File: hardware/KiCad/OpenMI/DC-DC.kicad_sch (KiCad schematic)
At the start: 37 parts, among them Q4 GAN7R0-150LBEZ, Q5 GAN7R0-150LBEZ, U3 1EDN7550B, U4 1EDN7550B

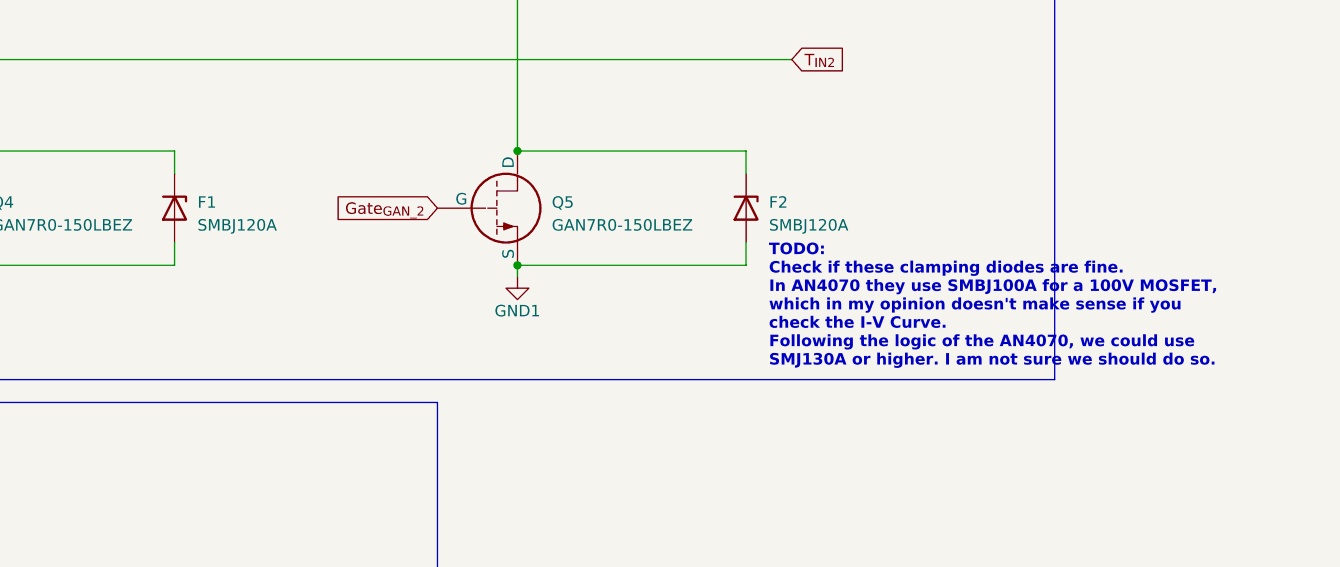
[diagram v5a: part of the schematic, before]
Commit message: fix(hw): change GaN FET protection from `SMBJ120A` to `SMBJ100A`
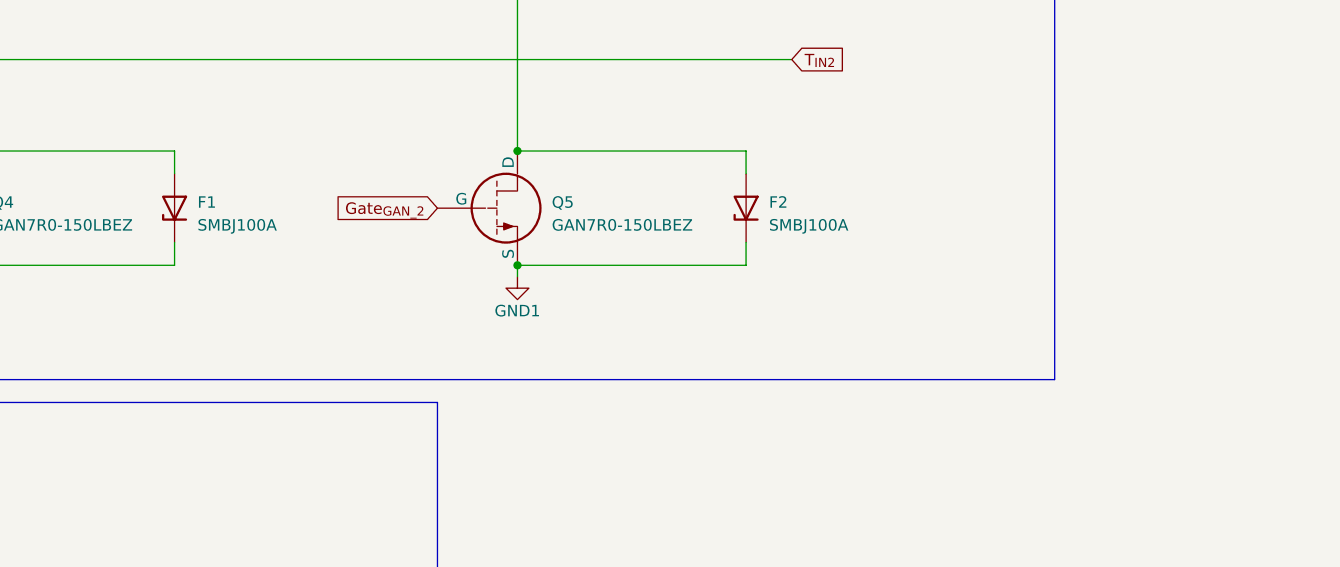
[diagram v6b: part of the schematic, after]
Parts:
- removed F1, F2: SMBJ120A, Diode_SMD:D_SMB, symbol _Diode_TVS:SMBJ120A
- added F1, F2: SMBJ100A, Diode_SMD:D_SMB, symbol _Diode_TVS:SMBJ100A
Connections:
- net GND1: now also F1.1 (K), F2.1 (K)
- net T_{IN1}: now also F2.2 (A)
- net T_{IN2}: now also F1.2 (A)
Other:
- note removed: "TODO: Check if these clamping diodes are fine. In AN4070 they use SMBJ100A for a 100V MOSFET, which in my opinion doesn't make sense if you check the I-V Curve. Following the logic of the AN4070, we could use SMJ130A or higher. I am not sure we should do so."
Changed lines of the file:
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@@
     (effects (font (size 1.27 1.27)) (justify left bottom))
-  )
-  (text "TODO:\nCheck if these clamping diodes are fine.\nIn AN4070 they use SMBJ100A for a 100V MOSFET,\nwhich in my opinion doesn't make sense if you \ncheck the I-V Curve.\nFollowing the logic of the AN4070, we could use\nSMJ130A or higher. I am not sure we should do so."
-    (at 336.55 160.02 0)
-    (effects (font (size 1.27 1.27) bold (color 255 0 0 1)) (justify left bottom))
   )
   (text "The GAN7R0-150LBEZ has a input capacitance of \n C_{iss} = 865 pF\nThe gate driver 1EDN7550B has rise times of\n t_{rise_1.8nF} = 6.5 ns\n t_{rise_200pF} = 1 ns\nSo using the GAN7R0-150LBEZ with the 1EDN7550B we can roughly asume:\n t_{rise_865pf} = (6.5 ns - 1 ns) / (1800 pF - 200 pF) * 865 pF  \n            = 2.97 ns\nThis results in\n  t_{charge_QGS} = 2.97 ns + 1.7 nC / 4 A  = 3.395 ns,\nwhich is\n  t_{charge_QGS} / T_{on_minimal} = 3.395 ns / 2000 ns ≈ 0.0017,\nso the rise time is at maximum 0.17% of the period time.\nThe results for the fall time should be roughly similar.\n\nSimulating this in LTSpice with\n  R_{Gate_SNK} = 2.2 Ω\n  R_{Gate_SRC} = 0.5 Ω\nresults in the following times (measuring V_{GS} from 10% to 90%)\n  t_{charge_QGS} = 8.44 ns     → 0.42% of period time\n  t_{discharge_QGS} = 2.59 ns   → 0.13% of period time"
@@
     )
   )
+  (symbol (lib_id "_Diode_TVS:SMBJ100A") (at 334.01 142.24 90) (unit 1)
+    (in_bom yes) (on_board yes) (dnp no) (fields_autoplaced)
+    (property "Reference" "F2" (at 336.55 141.605 90)
+      (effects (font (size 1.27 1.27)) (justify right))
+    )
+    (property "Value" "SMBJ100A" (at 336.55 144.145 90)
+      (effects (font (size 1.27 1.27)) (justify right))
+    )
+    (property "Footprint" "Diode_SMD:D_SMB" (at 334.01 142.24 0)
+      (effects (font (size 1.27 1.27)) hide)
+    )
+    (property "Datasheet" "https://www.mouser.de/datasheet/2/240/Littelfuse_TVS_Diode_SMBJ_Datasheet_pdf-1108540.pdf" (at 334.01 142.24 0)
+      (effects (font (size 1.27 1.27)) hide)
+    )
+    (property "MF" "Littelfuse" (at 334.01 142.24 0)
+      (effects (font (size 1.27 1.27)) hide)
+    )
+    (property "MPN" "SMBJ100A" (at 334.01 142.24 0)
+      (effects (font (size 1.27 1.27)) hide)
+    )
+    (property "OC_CONRAD" "" (at 334.01 142.24 0)
+      (effects (font (size 1.27 1.27)) hide)
+    )
+    (property "OC_FARNELL" "" (at 334.01 142.24 0)
+      (effects (font (size 1.27 1.27)) hide)
+    )
+    (property "OC_LCSC" "C151249" (at 334.01 142.24 0)
+      (effects (font (size 1.27 1.27)) hide)
+    )
+    (property "OC_MOUSER" "576-SMBJ100A" (at 334.01 142.24 0)
+      (effects (font (size 1.27 1.27)) hide)
+    )
+    (property "OC_REICHELT" "" (at 334.01 142.24 0)
+      (effects (font (size 1.27 1.27)) hide)
+    )
+    (pin "1")
+    (pin "2")
+    (instances
+      (project "OpenMI"
+        (path "/2d959e19-1572-42a0-a8fd-da8463ad4e66/efbfb180-c2bb-45aa-ab04-e5a4cb37fddc"
+          (reference "F2") (unit 1)
+        )
+      )
+    )
+  )
   (symbol (lib_id "power:+5V") (at 270.51 72.39 0) (unit 1)
     (in_bom yes) (on_board yes) (dnp no) (fields_autoplaced)
@@
         (path "/2d959e19-1572-42a0-a8fd-da8463ad4e66/efbfb180-c2bb-45aa-ab04-e5a4cb37fddc"
           (reference "R25") (unit 1)
+        )
+      )
+    )
+  )
+  (symbol (lib_id "_Diode_TVS:SMBJ100A") (at 270.51 142.24 90) (unit 1)
+    (in_bom yes) (on_board yes) (dnp no) (fields_autoplaced)
+    (property "Reference" "F1" (at 273.05 141.605 90)
+      (effects (font (size 1.27 1.27)) (justify right))
+    )
+    (property "Value" "SMBJ100A" (at 273.05 144.145 90)
+      (effects (font (size 1.27 1.27)) (justify right))
+    )
+    (property "Footprint" "Diode_SMD:D_SMB" (at 270.51 142.24 0)
+      (effects (font (size 1.27 1.27)) hide)
+    )
+    (property "Datasheet" "https://www.mouser.de/datasheet/2/240/Littelfuse_TVS_Diode_SMBJ_Datasheet_pdf-1108540.pdf" (at 270.51 142.24 0)
+      (effects (font (size 1.27 1.27)) hide)
+    )
+    (property "MF" "Littelfuse" (at 270.51 142.24 0)
+      (effects (font (size 1.27 1.27)) hide)
+    )
+    (property "MPN" "SMBJ100A" (at 270.51 142.24 0)
+      (effects (font (size 1.27 1.27)) hide)
+    )
+    (property "OC_CONRAD" "" (at 270.51 142.24 0)
+      (effects (font (size 1.27 1.27)) hide)
+    )
+    (property "OC_FARNELL" "" (at 270.51 142.24 0)
+      (effects (font (size 1.27 1.27)) hide)
+    )
+    (property "OC_LCSC" "C151249" (at 270.51 142.24 0)
+      (effects (font (size 1.27 1.27)) hide)
+    )
+    (property "OC_MOUSER" "576-SMBJ100A" (at 270.51 142.24 0)
+      (effects (font (size 1.27 1.27)) hide)
+    )
+    (property "OC_REICHELT" "" (at 270.51 142.24 0)
+      (effects (font (size 1.27 1.27)) hide)
+    )
+    (pin "1")
+    (pin "2")
+    (instances
+      (project "OpenMI"
+        (path "/2d959e19-1572-42a0-a8fd-da8463ad4e66/efbfb180-c2bb-45aa-ab04-e5a4cb37fddc"
+          (reference "F1") (unit 1)
         )
       )
@@
         )
       )
-    )
-  )
-  (symbol (lib_id "_Diode_TVS:SMBJ120A") (at 334.01 142.24 270) (unit 1)
-    (in_bom yes) (on_board yes) (dnp no) (fields_autoplaced)
-    (property "Reference" "F2" (at 336.55 141.605 90)
-      (effects (font (size 1.27 1.27)) (justify left))
-    )
-    (property "Value" "SMBJ120A" (at 336.55 144.145 90)
-      (effects (font (size 1.27 1.27)) (justify left))
-    )
-    (property "Footprint" "Diode_SMD:D_SMB" (at 334.01 142.24 0)
-      (effects (font (size 1.27 1.27)) hide)
-    )
-    (property "Datasheet" "https://www.mouser.de/datasheet/2/240/Littelfuse_TVS_Diode_SMBJ_Datasheet_pdf-1108540.pdf" (at 334.01 142.24 0)
-      (effects (font (size 1.27 1.27)) hide)
-    )
-    (property "MF" "Littelfuse" (at 334.01 142.24 0)
-      (effects (font (size 1.27 1.27)) hide)
-    )
-    (property "MPN" "SMBJ120A" (at 334.01 142.24 0)
-      (effects (font (size 1.27 1.27)) hide)
-    )
-    (property "OC_CONRAD" "" (at 334.01 142.24 0)
-      (effects (font (size 1.27 1.27)) hide)
-    )
-    (property "OC_FARNELL" "" (at 334.01 142.24 0)
-      (effects (font (size 1.27 1.27)) hide)
-    )
-    (property "OC_LCSC" "C224005" (at 334.01 142.24 0)
-      (effects (font (size 1.27 1.27)) hide)
-    )
-    (property "OC_MOUSER" "576-SMBJ120A" (at 334.01 142.24 0)
-      (effects (font (size 1.27 1.27)) hide)
-    )
-    (property "OC_REICHELT" "" (at 334.01 142.24 0)
-      (effects (font (size 1.27 1.27)) hide)
-    )
-    (pin "1")
-    (pin "2")
-    (instances
-      (project "OpenMI"
-        (path "/2d959e19-1572-42a0-a8fd-da8463ad4e66/efbfb180-c2bb-45aa-ab04-e5a4cb37fddc"
-          (reference "F2") (unit 1)
-        )
-      )
-    )
-  )
-  (symbol (lib_id "_Diode_TVS:SMBJ120A") (at 270.51 142.24 270) (unit 1)
-    (in_bom yes) (on_board yes) (dnp no) (fields_autoplaced)
-    (property "Reference" "F1" (at 273.05 141.605 90)
-      (effects (font (size 1.27 1.27)) (justify left))
-    )
-    (property "Value" "SMBJ120A" (at 273.05 144.145 90)
-      (effects (font (size 1.27 1.27)) (justify left))
-    )
-    (property "Footprint" "Diode_SMD:D_SMB" (at 270.51 142.24 0)
-      (effects (font (size 1.27 1.27)) hide)
-    )
-    (property "Datasheet" "https://www.mouser.de/datasheet/2/240/Littelfuse_TVS_Diode_SMBJ_Datasheet_pdf-1108540.pdf" (at 270.51 142.24 0)
-      (effects (font (size 1.27 1.27)) hide)
-    )
-    (property "MF" "Littelfuse" (at 270.51 142.24 0)
-      (effects (font (size 1.27 1.27)) hide)
-    )
-    (property "MPN" "SMBJ120A" (at 270.51 142.24 0)
-      (effects (font (size 1.27 1.27)) hide)
-    )
-    (property "OC_CONRAD" "" (at 270.51 142.24 0)
-      (effects (font (size 1.27 1.27)) hide)
-    )
-    (property "OC_FARNELL" "" (at 270.51 142.24 0)
-      (effects (font (size 1.27 1.27)) hide)
-    )
-    (property "OC_LCSC" "C224005" (at 270.51 142.24 0)
-      (effects (font (size 1.27 1.27)) hide)
-    )
-    (property "OC_MOUSER" "576-SMBJ120A" (at 270.51 142.24 0)
-      (effects (font (size 1.27 1.27)) hide)
-    )
-    (property "OC_REICHELT" "" (at 270.51 142.24 0)
-      (effects (font (size 1.27 1.27)) hide)
-    )
-    (pin "1")
-    (pin "2")
-    (instances
-      (project "OpenMI"
-        (path "/2d959e19-1572-42a0-a8fd-da8463ad4e66/efbfb180-c2bb-45aa-ab04-e5a4cb37fddc"
-          (reference "F1") (unit 1)
-        )
-      )

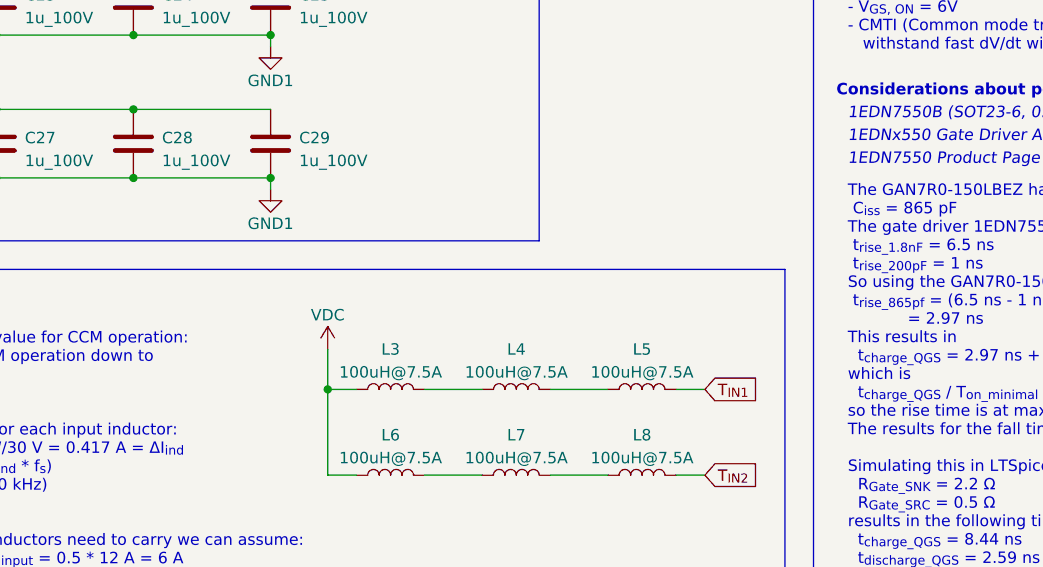
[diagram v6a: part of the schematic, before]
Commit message: docs: Adds to-do to remember high current, high frequency inductors
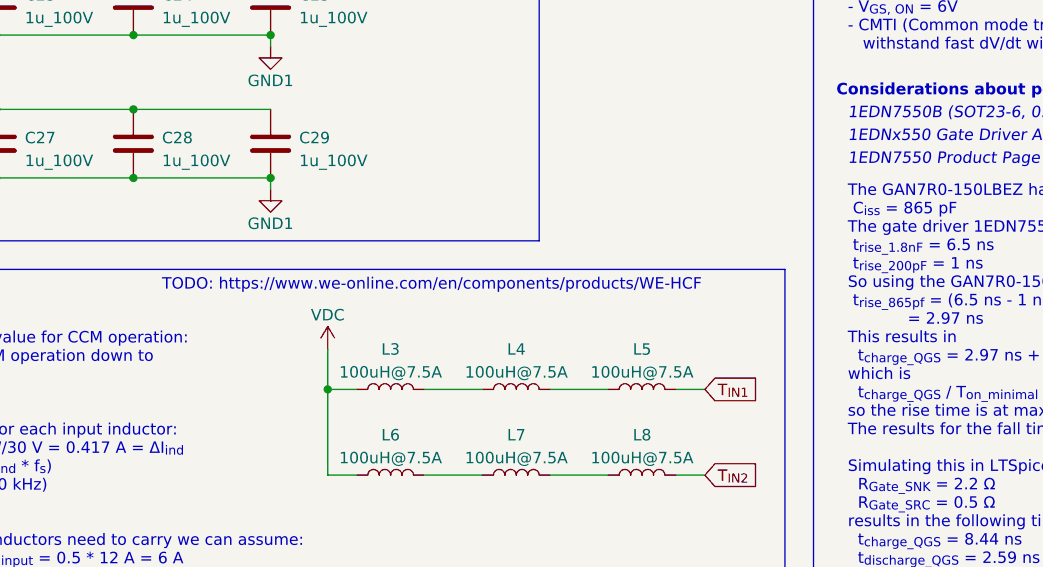
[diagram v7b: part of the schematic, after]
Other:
- note added: "TODO: https://www.we-online.com/en/components/products/WE-HCF"
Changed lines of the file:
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@@
     (effects (font (size 2 2) bold) (justify left bottom))
+  )
+  (text "TODO: https://www.we-online.com/en/components/products/WE-HCF"
+    (at 66.04 102.87 0)
+    (effects (font (size 1.27 1.27) (color 255 0 0 1)) (justify left bottom))
   )
   (text "1EDN7116U, 2A, 3ns, 200V" (at 142.24 146.05 0)

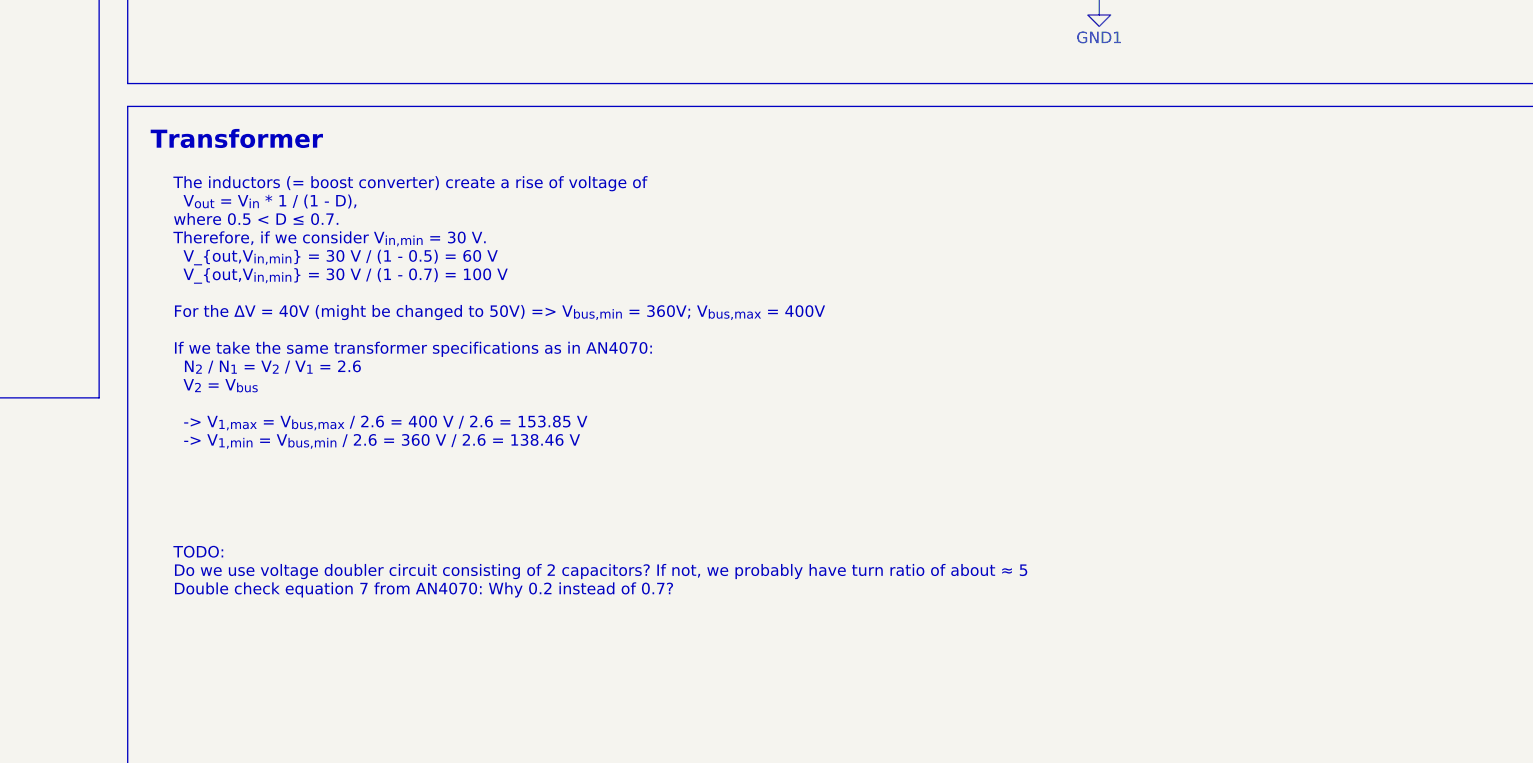
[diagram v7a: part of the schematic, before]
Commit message: docs: reworks considerations for transformer turn ratio
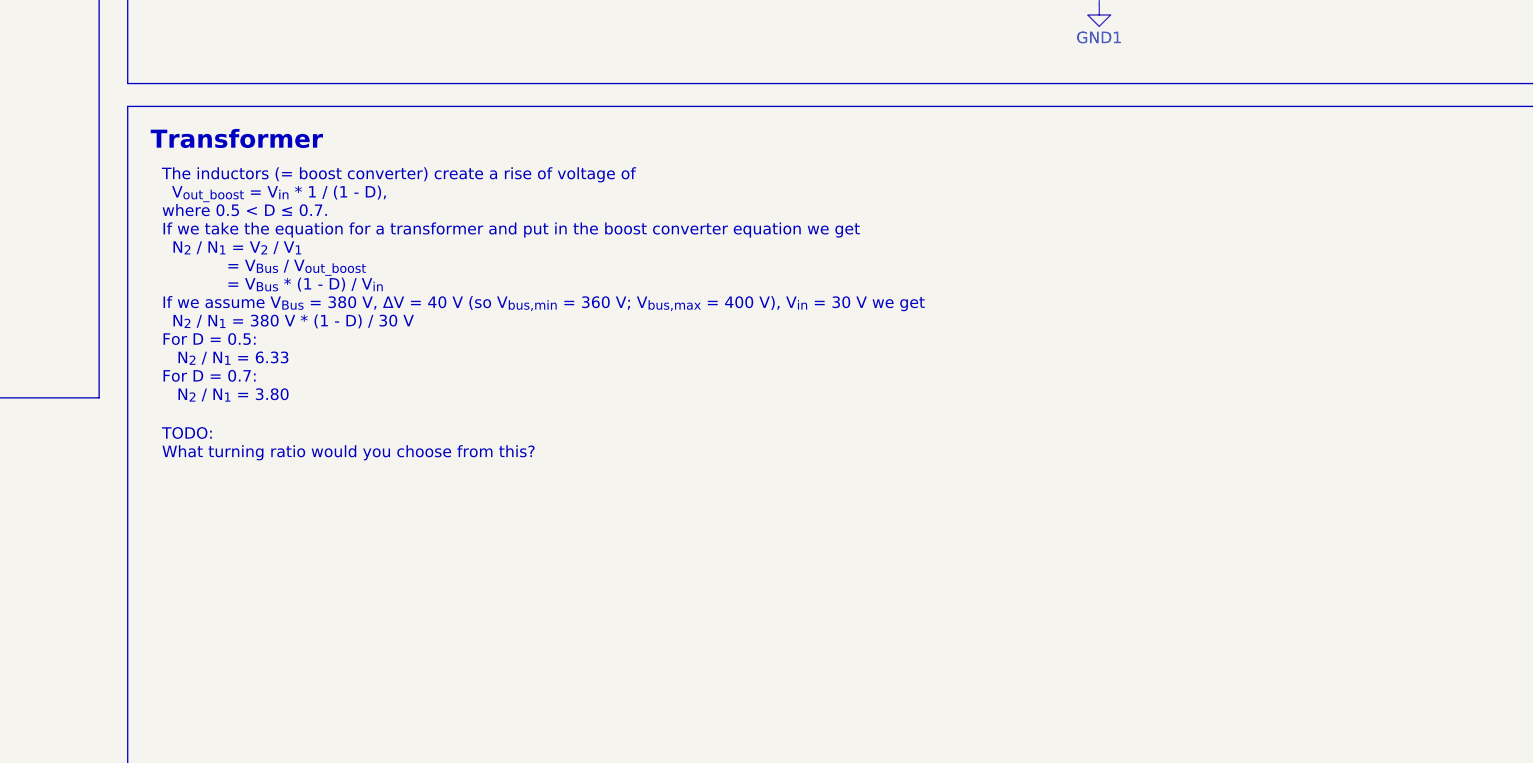
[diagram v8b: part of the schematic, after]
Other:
- note added: "TODO: What turning ratio would you choose from this?"
- note added: "The inductors (= boost converter) create a rise of voltage of V_{out_boost} = V_{in} * 1 / (1 - D), where 0.5 < D ≤ 0.7. If we take the equation for a transformer and put in the boost converter equation we get N_{2} / N_{1} = V_{2} / V_{1} = V_{Bus} / V_{out_boost} = V_{Bus} * (1 - D) / V_{in} If we assume V_{Bus} = 380 V, ΔV = 40 V (so V_{bus,min} = 360 V; V_{bus,max} = 400 V), V_{in} = 30 V we 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"
- note removed: "TODO: Do we use voltage doubler circuit consisting of 2 capacitors? If not, we probably have turn ratio of about ≈ 5 Double check equation 7 from AN4070: Why 0.2 instead of 0.7?"
- note removed: "The inductors (= boost converter) create a rise of voltage of V_{out} = V_{in} * 1 / (1 - D), where 0.5 < D ≤ 0.7. Therefore, if we consider V_{in,min} = 30 V. V_{out,V_{in,min}} = 30 V / (1 - 0.5) = 60 V V_{out,V_{in,min}} = 30 V / (1 - 0.7) = 100 V For the ΔV = 40V (might be changed to 50V) => V_{bus,min} = 360V; V_{bus,max} = 400V If we take the same transformer specifications as in AN4070: N_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"
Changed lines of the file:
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@@
     (effects (font (size 1.27 1.27)) (justify left bottom))
   )
-  (text "The inductors (= boost converter) create a rise of voltage of\n  V_{out} = V_{in} * 1 / (1 - D),\nwhere 0.5 < D ≤ 0.7.\nTherefore, if we consider V_{in,min} = 30 V.\n  V_{out,V_{in,min}} = 30 V / (1 - 0.5) = 60 V  \n  V_{out,V_{in,min}} = 30 V / (1 - 0.7) = 100 V\n\nFor the ΔV = 40V (might be changed to 50V) => V_{bus,min} = 360V; V_{bus,max} = 400V\n\nIf we take the same transformer specifications as in AN4070:\n  N_{2} / N_{1} = V_{2} / V_{1} = 2.6\n  V_{2} = V_{bus}\n\n  -> V_{1,max} = V_{bus,max} / 2.6 = 400 V / 2.6 = 153.85 V\n  -> V_{1,min} = V_{bus,min} / 2.6 = 360 V / 2.6 = 138.46 V "
-    (at 143.51 201.93 0)
+  (text "The inductors (= boost converter) create a rise of voltage of\n  V_{out_boost} = V_{in} * 1 / (1 - D),\nwhere 0.5 < D ≤ 0.7.\nIf we take the equation for a transformer and put in the boost converter equation we get\n  N_{2} / N_{1} = V_{2} / V_{1} \n             = V_{Bus} / V_{out_boost} \n             = V_{Bus} * (1 - D) / V_{in}\nIf we assume V_{Bus} = 380 V, ΔV = 40 V (so V_{bus,min} = 360 V; V_{bus,max} = 400 V), V_{in} = 30 V we get\n  N_{2} / N_{1} = 380 V * (1 - D) / 30 V\nFor D = 0.5:\n   N_{2} / N_{1} = 6.33\nFor D = 0.7:\n   N_{2} / N_{1} = 3.80"
+    (at 142.24 196.85 0)
     (effects (font (size 1.27 1.27)) (justify left bottom))
   )
-  (text "TODO:\nDo we use voltage doubler circuit consisting of 2 capacitors? If not, we probably have turn ratio of about ≈ 5\nDouble check equation 7 from AN4070: Why 0.2 instead of 0.7? \n"
-    (at 143.51 218.44 0)
+  (text "TODO:\nWhat turning ratio would you choose from this?\n"
+    (at 142.24 203.2 0)
     (effects (font (size 1.27 1.27) (color 255 0 0 1)) (justify left bottom))
   )
